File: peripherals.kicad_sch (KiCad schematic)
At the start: 17 parts, among them J6 Conn_01x04, J7 Conn_01x06, J8 Conn_01x06, U10 MPU-6050, U11 TB6612FNG

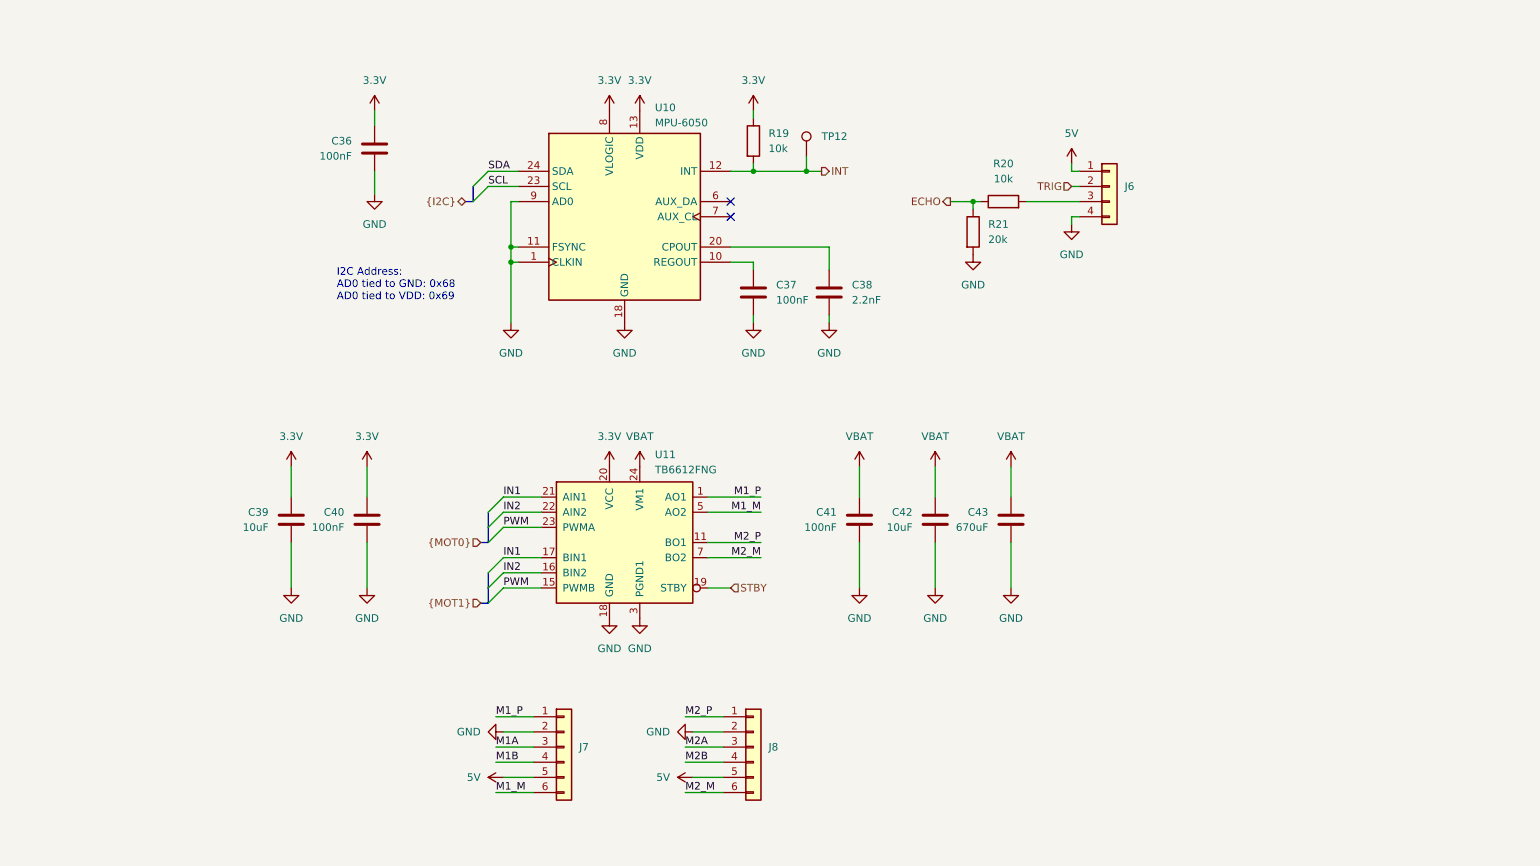
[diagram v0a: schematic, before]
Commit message: Correct voltage level translation
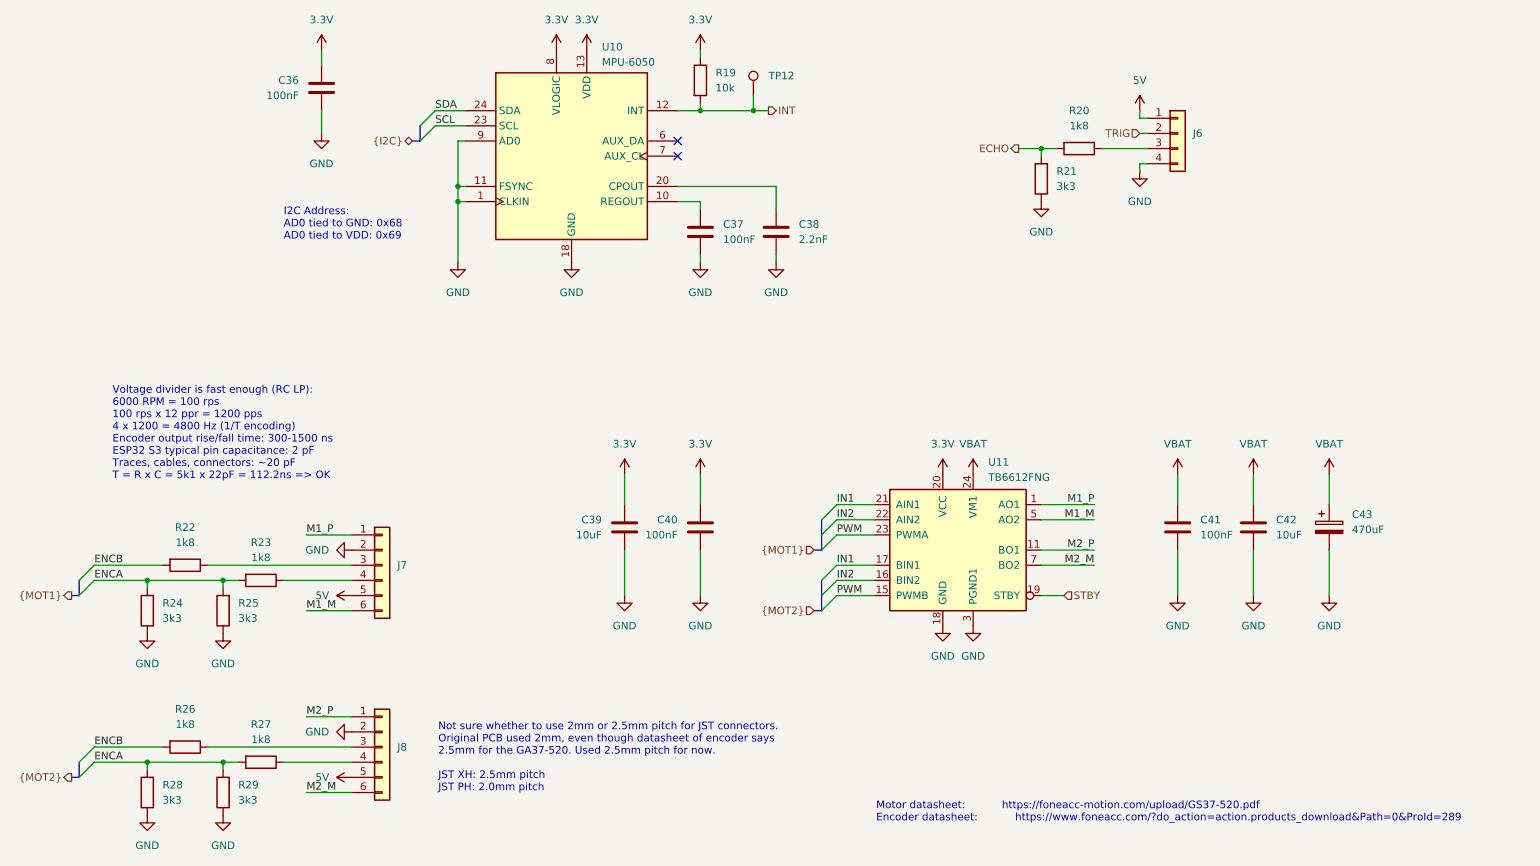
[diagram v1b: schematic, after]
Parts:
- removed C43: 670uF, Capacitor_SMD:C_0805_2012Metric_Pad1.18x1.45mm_HandSolder, symbol Device:C
- added C43: 470uF, symbol Device:C_Polarized
- added R22, R23, R26, R27: 1k8, symbol Device:R
- added R24, R25, R28, R29: 3k3, symbol Device:R
- J7, J8: footprint Connector_JST:JST_PH_S6B-PH-SM4-TB_1x06-1MP_P2.00mm_Horizontal -> Connector_JST:JST_XH_S6B-XH-SM4-TB_1x06-1MP_P2.50mm_Horizontal; LCSC Part (none) -> C191914
- R20: value 10k -> 1k8
- R21: value 20k -> 3k3
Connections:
- net ECHO: now also R20.2, R21.2; no longer R20.1, R21.1
- net GND: now also R21.1, C43.2, R24.1, R25.1, R28.1, R29.1; no longer R21.2
- net VBAT: now also C43.1
- net at J6.3 (Pin_3): now also R20.1; no longer R20.2
- net M1A: no longer names the net of J7.3 (Pin_3)
- net M1A: now also R22.1
- net M1B: no longer names the net of J7.4 (Pin_4)
- net M1B: now also R23.1
- net M2A: no longer names the net of J8.3 (Pin_3)
- net M2A: now also R26.1
- net M2B: no longer names the net of J8.4 (Pin_4)
- net M2B: now also R27.1
- new net ENCA: R23.2, R24.2, R25.2, R27.2, R28.2, R29.2
- new net ENCB: R22.2, R26.2
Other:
- note added: "Motor datasheet: Encoder datasheet:"
- note added: "Not sure whether to use 2mm or 2.5mm pitch for JST connectors. Original PCB used 2mm, even though datasheet of encoder says 2.5mm for the GA37-520. Used 2.5mm pitch for now. JST XH: 2.5mm pitch JST PH: 2.0mm pitch"
- note added: "Voltage divider is fast enough (RC LP): 6000 RPM = 100 rps 100 rps x 12 ppr = 1200 pps 4 x 1200 = 4800 Hz (1/T encoding) Encoder output rise/fall time: 300-1500 ns ESP32 S3 typical pin capacitance: 2 pF Traces, cables, connectors: ~20 pF T = R x C = 5k1 x 22pF = 112.2ns => OK"
- note added: "https://foneacc-motion.com/upload/GS37-520.pdf"
- note added: "https://www.foneacc.com/?do_action=action.products_download&Path=0&ProId=289"
- moved on the sheet: C36, C37, C38, C39, C40, C41, C42, J6, J7, R19, TP12, U10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

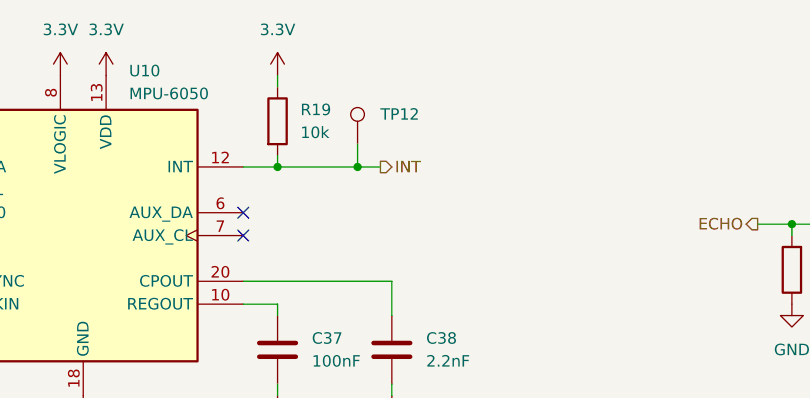
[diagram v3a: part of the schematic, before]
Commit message: Move fuse to correct location
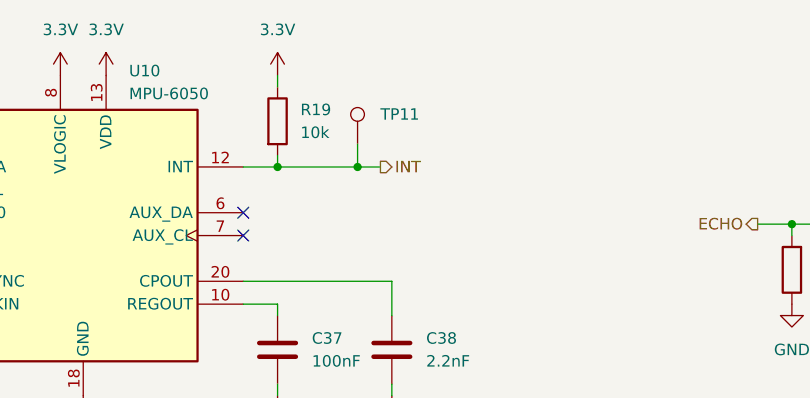
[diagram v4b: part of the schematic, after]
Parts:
- renumbered TP12 to TP11
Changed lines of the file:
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@@
 		(dnp no)
 		(fields_autoplaced yes)
-		(property "Reference" "TP12"
+		(property "Reference" "TP11"
 			(at 158.75 39.8779 0)
 			(effects
@@
 			(project "Tumbler2_Redesign"
 				(path "/f3fd8d79-9d35-4c04-811e-2697a2740958/f8585a58-8128-4c19-a894-5097be4fe7b3"
-					(reference "TP12")
+					(reference "TP11")
 					(unit 1)
 				)

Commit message: Assign footprints and parts
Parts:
- added C36: 100nF, Capacitor_SMD:C_0603_1608Metric_Pad1.08x0.95mm_HandSolder, symbol Device:C
- C37: renamed from C36; value 100nF -> 10nF; footprint Capacitor_SMD:C_0402_1005Metric_Pad0.74x0.62mm_HandSolder -> Capacitor_SMD:C_0603_1608Metric_Pad1.08x0.95mm_HandSolder; LCSC Part (none) -> C100042
- C38: renamed from C37; footprint Capacitor_SMD:C_0402_1005Metric_Pad0.74x0.62mm_HandSolder -> Capacitor_SMD:C_0603_1608Metric_Pad1.08x0.95mm_HandSolder; LCSC Part (none) -> C14663
- C39: renamed from C38; footprint Capacitor_SMD:C_0402_1005Metric_Pad0.74x0.62mm_HandSolder -> Capacitor_SMD:C_0603_1608Metric_Pad1.08x0.95mm_HandSolder; LCSC Part (none) -> C107043
- C40: renamed from C39; LCSC Part (none) -> C96446
- C41: renamed from C40; footprint Capacitor_SMD:C_0402_1005Metric_Pad0.74x0.62mm_HandSolder -> Capacitor_SMD:C_0603_1608Metric_Pad1.08x0.95mm_HandSolder; LCSC Part (none) -> C14663
- C42: renamed from C41; footprint Capacitor_SMD:C_0402_1005Metric_Pad0.74x0.62mm_HandSolder -> Capacitor_SMD:C_0603_1608Metric_Pad1.08x0.95mm_HandSolder; LCSC Part (none) -> C14663
- C43: renamed from C42; LCSC Part (none) -> C96446
- C44: renamed from C43; value 470uF -> 220uF; footprint (none) -> Capacitor_SMD:CP_Elec_10x10; LCSC Part (none) -> C250054
- J6: LCSC Part (none) -> C5116530
- R19: footprint (none) -> Resistor_SMD:R_0603_1608Metric_Pad0.98x0.95mm_HandSolder; LCSC Part (none) -> C98220
- R20, R22, R23, R26, R27: footprint (none) -> Resistor_SMD:R_0603_1608Metric_Pad0.98x0.95mm_HandSolder; LCSC Part (none) -> C185354
- R21, R24, R25, R28, R29: footprint (none) -> Resistor_SMD:R_0603_1608Metric_Pad0.98x0.95mm_HandSolder; LCSC Part (none) -> C108078
- TP11: footprint (none) -> TestPoint:TestPoint_Pad_D1.5mm
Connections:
- net 3.3V: now also C36.1
- net GND: now also C36.2
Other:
- moved on the sheet: C40, C41, C42, C43, C44, U11

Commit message: De-cascade buck converters
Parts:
- renumbered R19 to R20, R20 to R21, R21 to R22, R22 to R23, R23 to R24, R24 to R25, R25 to R26, R26 to R27, R27 to R28, R28 to R29, R29 to R30, TP11 to TP10

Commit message: Break out motor encoder signals
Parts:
- renumbered C36 to C37, C37 to C38, C38 to C39, C39 to C40, C40 to C41, C41 to C42, C42 to C43, C43 to C44, C44 to C45, J6 to J7, J7 to J8, J8 to J9

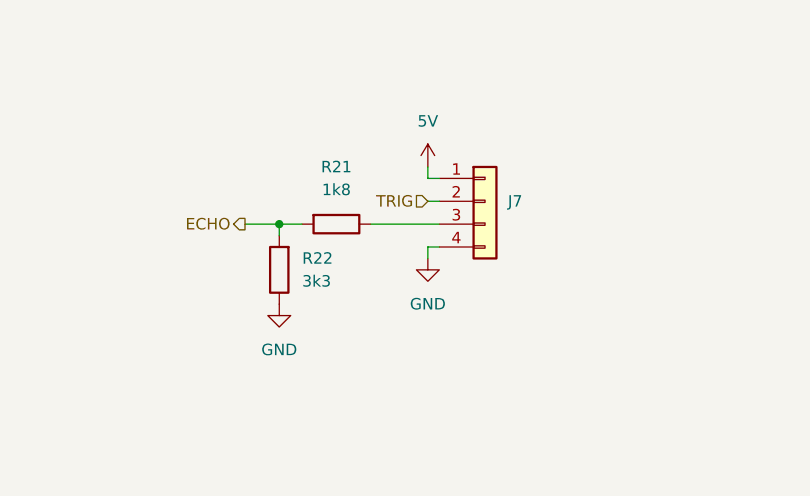
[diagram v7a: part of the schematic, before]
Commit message: Add test points for ultrasonic sensor
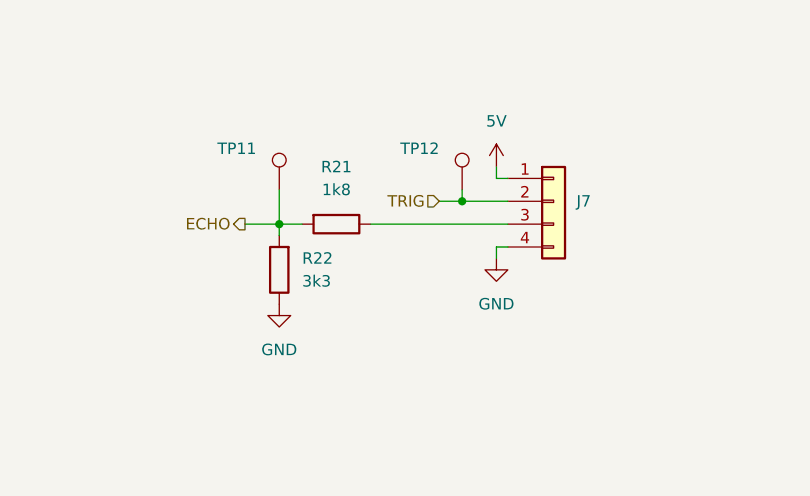
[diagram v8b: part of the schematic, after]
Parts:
- added TP11, TP12: TestPoint, symbol Connector:TestPoint
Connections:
- net ECHO: now also TP11.1
- net TRIG: now also TP12.1
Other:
- moved on the sheet: J7
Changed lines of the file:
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@@
 	)
 	(junction
+		(at 224.79 49.53)
+		(diameter 0)
+		(color 0 0 0 0)
+	)
+	(junction
 		(at 54.61 154.94)
 		(diameter 0)
@@
 	(wire
 		(pts
-			(xy 220.98 54.61) (xy 222.25 54.61)
+			(xy 228.6 54.61) (xy 229.87 54.61)
 		)
 		(stroke
@@
 	(wire
 		(pts
+			(xy 224.79 48.26) (xy 224.79 49.53)
+		)
+		(stroke
+			(width 0)
+			(type default)
+		)
+	)
+	(wire
+		(pts
 			(xy 143.51 58.42) (xy 160.02 58.42)
 		)
@@
 	(wire
 		(pts
-			(xy 220.98 46.99) (xy 220.98 45.72)
+			(xy 228.6 46.99) (xy 228.6 45.72)
 		)
 		(stroke
@@
 	(wire
 		(pts
-			(xy 220.98 46.99) (xy 222.25 46.99)
+			(xy 228.6 46.99) (xy 229.87 46.99)
 		)
 		(stroke
@@
 		)
 	)
+	(wire
+		(pts
+			(xy 204.47 48.26) (xy 204.47 52.07)
+		)
+		(stroke
+			(width 0)
+			(type default)
+		)
+	)
 	(bus
 		(pts
@@
 	(wire
 		(pts
-			(xy 214.63 52.07) (xy 222.25 52.07)
-		)
-		(stroke
-			(width 0)
-			(type default)
-		)
-	)
-	(wire
-		(pts
 			(xy 106.68 71.12) (xy 106.68 60.96)
 		)
@@
 	(wire
 		(pts
-			(xy 220.98 49.53) (xy 222.25 49.53)
+			(xy 222.25 49.53) (xy 224.79 49.53)
 		)
 		(stroke
@@
 	(wire
 		(pts
-			(xy 220.98 55.88) (xy 220.98 54.61)
+			(xy 228.6 55.88) (xy 228.6 54.61)
 		)
 		(stroke
@@
 		)
 	)
+	(wire
+		(pts
+			(xy 224.79 49.53) (xy 229.87 49.53)
+		)
+		(stroke
+			(width 0)
+			(type default)
+		)
+	)
 	(bus
 		(pts
@@
 	(wire
 		(pts
+			(xy 214.63 52.07) (xy 229.87 52.07)
+		)
+		(stroke
+			(width 0)
+			(type default)
+		)
+	)
+	(wire
+		(pts
 			(xy 248.92 119.38) (xy 248.92 127)
 		)
@@
 	(hierarchical_label "TRIG"
 		(shape input)
-		(at 220.98 49.53 180)
+		(at 222.25 49.53 180)
 		(effects
 			(font
@@
 	(symbol
 		(lib_id "Connector_Generic:Conn_01x04")
-		(at 227.33 49.53 0)
+		(at 234.95 49.53 0)
 		(unit 1)
 		(exclude_from_sim no)
@@
 		(dnp no)
 		(property "Reference" "J7"
-			(at 229.87 49.5299 0)
+			(at 237.49 49.5299 0)
 			(effects
 				(font
@@
 		)
 		(property "Value" "Conn_01x04"
-			(at 229.87 52.0699 0)
+			(at 237.49 52.0699 0)
 			(effects
 				(font
@@
 		)
 		(property "Footprint" "Connector_PinHeader_2.54mm:PinHeader_1x04_P2.54mm_Vertical"
-			(at 227.33 49.53 0)
+			(at 234.95 49.53 0)
 			(effects
 				(font
@@
 		)
 		(property "Datasheet" "https://www.lcsc.com/datasheet/C5116530.pdf"
-			(at 227.33 49.53 0)
+			(at 234.95 49.53 0)
 			(effects
 				(font
@@
 		)
 		(property "Description" "Generic connector, single row, 01x04, script generated (kicad-library-utils/schlib/autogen/connector/)"
-			(at 227.33 49.53 0)
+			(at 234.95 49.53 0)
 			(effects
 				(font
@@
 		)
 		(property "LCSC Part" "C5116530"
-			(at 227.33 49.53 0)
+			(at 234.95 49.53 0)
 			(effects
 				(font
@@
 	)
 	(symbol
+		(lib_id "Connector:TestPoint")
+		(at 224.79 48.26 0)
+		(mirror y)
+		(unit 1)
+		(exclude_from_sim no)
+		(in_bom yes)
+		(on_board yes)
+		(dnp no)
+		(property "Reference" "TP12"
+			(at 222.25 43.6879 0)
+			(effects
+				(font
+					(size 1.27 1.27)
+				)
+				(justify left)
+			)
+		)
+		(property "Value" "TestPoint"
+			(at 222.25 46.2279 0)
+			(effects
+				(font
+					(size 1.27 1.27)
+				)
+				(justify left)
+				(hide yes)
+			)
+		)
+		(property "Footprint" ""
+			(at 219.71 48.26 0)
+			(effects
+				(font
+					(size 1.27 1.27)
+				)
+				(hide yes)
+			)
+		)
+		(property "Datasheet" "~"
+			(at 219.71 48.26 0)
+			(effects
+				(font
+					(size 1.27 1.27)
+				)
+				(hide yes)
+			)
+		)
+		(property "Description" "test point"
+			(at 224.79 48.26 0)
+			(effects
+				(font
+					(size 1.27 1.27)
+				)
+				(hide yes)
+			)
+		)
+		(pin "1"
+		)
+		(instances
+			(project "Tumbler2_Redesign"
+				(path "/f3fd8d79-9d35-4c04-811e-2697a2740958/f8585a58-8128-4c19-a894-5097be4fe7b3"
+					(reference "TP12")
+					(unit 1)
+				)
+			)
+		)
+	)
+	(symbol
 		(lib_id "Driver_Motor:TB6612FNG")
 		(at 186.69 119.38 0)
@@
 	)
 	(symbol
+		(lib_id "Connector:TestPoint")
+		(at 204.47 48.26 0)
+		(mirror y)
+		(unit 1)
+		(exclude_from_sim no)
+		(in_bom yes)
+		(on_board yes)
+		(dnp no)
+		(property "Reference" "TP11"
+			(at 201.93 43.6879 0)
+			(effects
+				(font
+					(size 1.27 1.27)
+				)
+				(justify left)
+			)
+		)
+		(property "Value" "TestPoint"
+			(at 201.93 46.2279 0)
+			(effects
+				(font
+					(size 1.27 1.27)
+				)
+				(justify left)
+				(hide yes)
+			)
+		)
+		(property "Footprint" ""
+			(at 199.39 48.26 0)
+			(effects
+				(font
+					(size 1.27 1.27)
+				)
+				(hide yes)
+			)
+		)
+		(property "Datasheet" "~"
+			(at 199.39 48.26 0)
+			(effects
+				(font
+					(size 1.27 1.27)
+				)
+				(hide yes)
+			)
+		)
+		(property "Description" "test point"
+			(at 204.47 48.26 0)
+			(effects
+				(font
+					(size 1.27 1.27)
+				)
+				(hide yes)
+			)
+		)
+		(pin "1"
+		)
+		(instances
+			(project ""
+				(path "/f3fd8d79-9d35-4c04-811e-2697a2740958/f8585a58-8128-4c19-a894-5097be4fe7b3"
+					(reference "TP11")
+					(unit 1)
+				)
+			)
+		)
+	)
+	(symbol
 		(lib_id "Device:R")
 		(at 54.61 160.02 180)
@@
 	(symbol
 		(lib_id "power:GND")
-		(at 220.98 55.88 0)
+		(at 228.6 55.88 0)
 		(unit 1)
 		(exclude_from_sim no)
@@
 		(fields_autoplaced yes)
 		(property "Reference" "#PWR0146"
-			(at 220.98 62.23 0)
+			(at 228.6 62.23 0)
 			(effects
 				(font
@@
 		)
 		(property "Value" "GND"
-			(at 220.98 60.96 0)
+			(at 228.6 60.96 0)
 			(effects
 				(font
@@
 		)
 		(property "Footprint" ""
-			(at 220.98 55.88 0)
+			(at 228.6 55.88 0)
 			(effects
 				(font
@@
 		)
 		(property "Datasheet" ""
-			(at 220.98 55.88 0)
+			(at 228.6 55.88 0)
 			(effects
 				(font
@@
 		)
 		(property "Description" "Power symbol creates a global label with name \"GND\" , ground"
-			(at 220.98 55.88 0)
+			(at 228.6 55.88 0)
 			(effects
 				(font
@@
 	(symbol
 		(lib_id "power:VCC")
-		(at 220.98 45.72 0)
+		(at 228.6 45.72 0)
 		(unit 1)
 		(exclude_from_sim no)
@@
 		(fields_autoplaced yes)
 		(property "Reference" "#PWR0143"
-			(at 220.98 49.53 0)
+			(at 228.6 49.53 0)
 			(effects
 				(font
@@
 		)
 		(property "Value" "5V"
-			(at 220.98 40.64 0)
+			(at 228.6 40.64 0)
 			(effects
 				(font
@@
 		)
 		(property "Footprint" ""
-			(at 220.98 45.72 0)
+			(at 228.6 45.72 0)
 			(effects
 				(font
@@
 		)
 		(property "Datasheet" ""
-			(at 220.98 45.72 0)
+			(at 228.6 45.72 0)
 			(effects
 				(font
@@
 		)
 		(property "Description" "Power symbol creates a global label with name \"VCC\""
-			(at 220.98 45.72 0)
+			(at 228.6 45.72 0)
 			(effects
 				(font
